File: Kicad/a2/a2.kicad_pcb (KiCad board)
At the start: 2 copper layers, 190 x 100 mm, 123 parts, among them J1 Conn_02x03_Odd_Even, J2 VGA, J3 AudioJack4, J4 Conn_02x17_Odd_Even, J6 Barrel Jack, J7 DE9_Plug, J8 DE9_Plug, SW1 Q, SW10 P, SW11 A, SW12 S, SW13 D, SW14 F, SW15 G, SW16 H, SW17 J, SW18 K, SW19 L, SW2 W, SW20 ENT, SW21 SHIFT, SW22 Z, SW23 X, SW24 C, SW25 V, SW26 B, SW27 N, SW28 M, SW29 SPACE, SW3 E, SW30 ALT, SW31 SW_Push, SW32 SW_SPDT, SW4 R, SW5 T, SW6 Y, SW7 U, SW8 I, SW9 O, U1 74HC590A, U10 74HC32, U11 74HC174, U12 74HC4520, U2 74HC590A, U3 62256, U4 SST39SF0x0, U5 W65C02SxP, U6 74HCT540, U7 74HC166, U8 74HC14, U9 74HC10, Y1 16Mhz

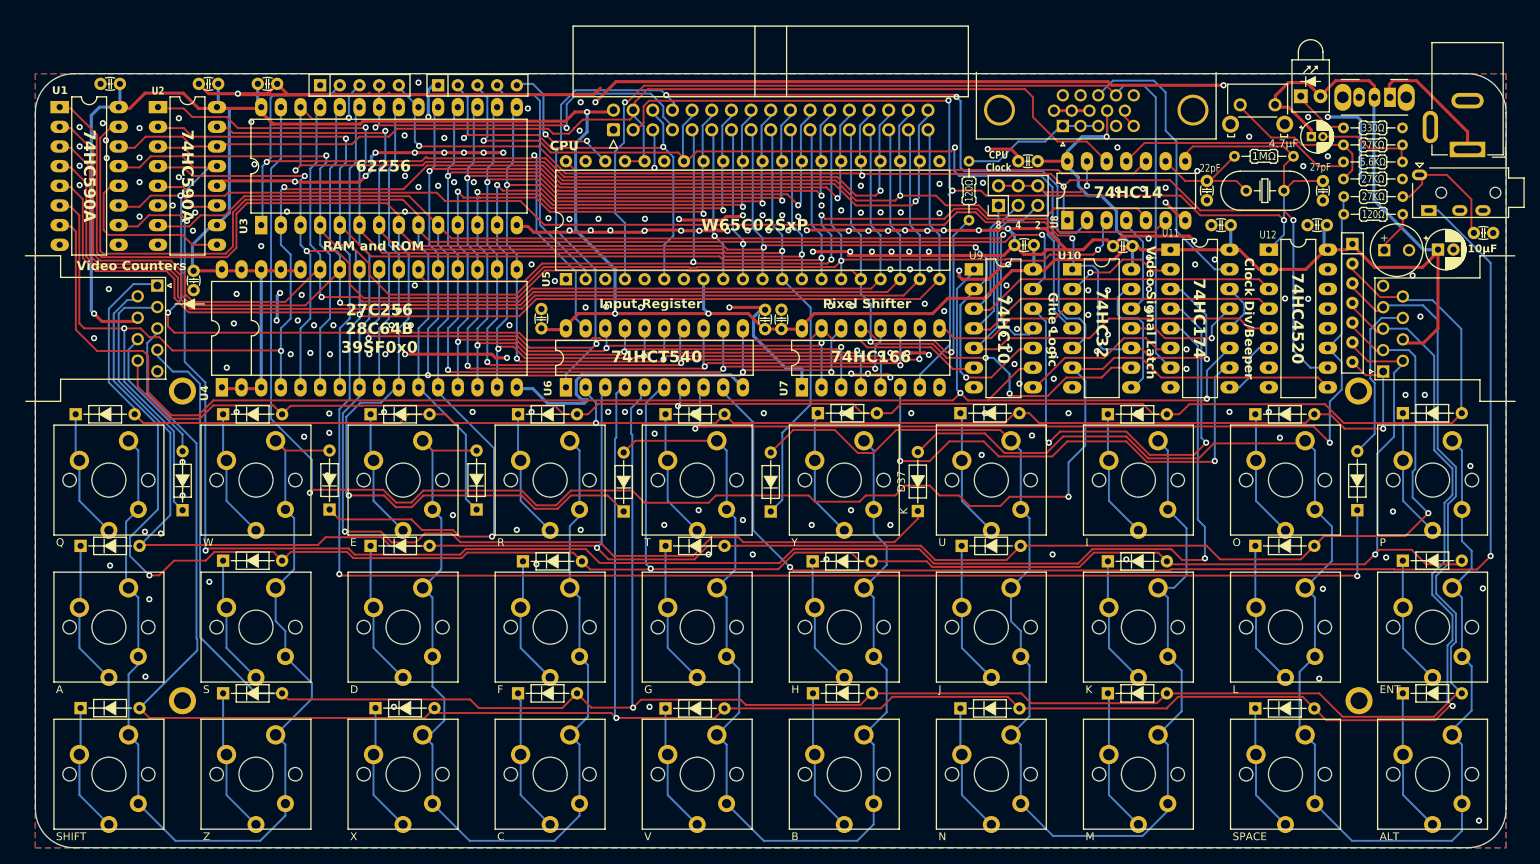
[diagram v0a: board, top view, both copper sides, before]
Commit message: add 2 more m2 screw posts
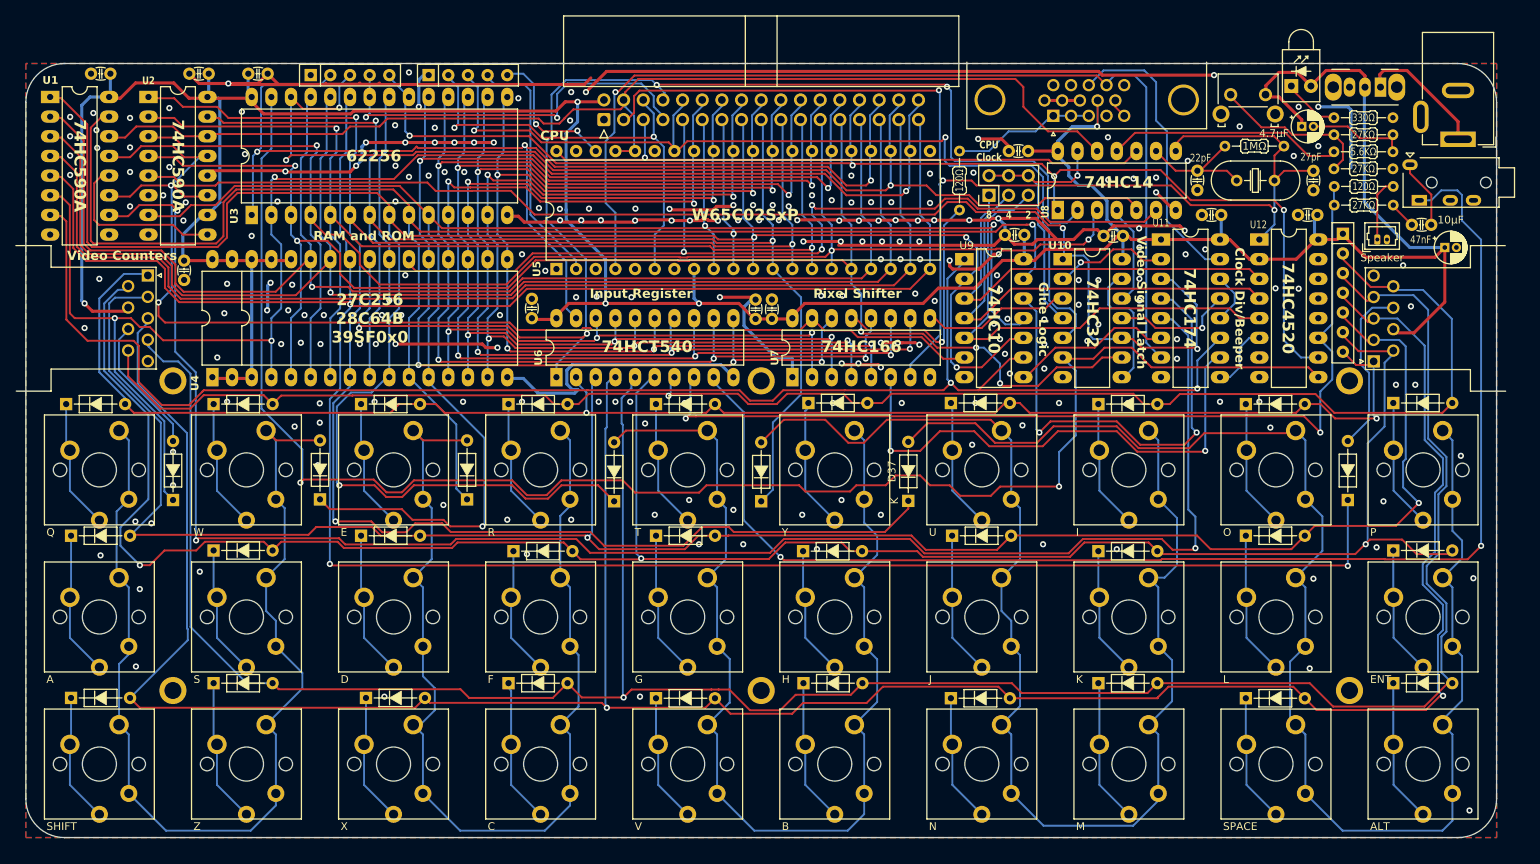
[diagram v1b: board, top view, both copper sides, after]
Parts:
- removed BZ1: Buzzer, Buzzer_Beeper:MagneticBuzzer_Kingstate_KCG0601
- added H5: M2, MountingHole:MountingHole_2.2mm_M2_ISO7380_Pad, F.Cu at (130.0, 116.0)
- added H6: M2, MountingHole:MountingHole_2.2mm_M2_ISO7380_Pad, F.Cu at (130.0, 76.0)
- added LS1: Speaker, Connector_Molex:Molex_PicoBlade_53047-0210_1x02_P1.25mm_Vertical, F.Cu at (209.6, 57.7)
- C16: footprint PCM_Capacitor_THT_AKL:CP_Radial_D5.0mm_P2.00mm -> PCM_Capacitor_THT_AKL:CP_Radial_D4.0mm_P1.50mm
- C17: value 100nF -> 47nF
- H1, H2, H3, H4: value MountingHole_Pad -> M2
- RN1: value R_Network06 -> 10KΩ
- RN2, RN3: value R_Network04 -> 1KΩ
- moved C17 5.61 mm to (216.6, 55.8), turned to 180 degrees
- moved R8 3.81 mm to (204.0, 50.9)
- moved D41 1.80 mm to (198.5, 37.9)
- moved D28 1.80 mm to (78.9, 117.0)
- moved C13 1.80 mm to (174.2, 57.3)
- moved C15 1.80 mm to (199.3, 54.6)
- moved D10 1.80 mm to (154.5, 78.9)
- moved D11 1.80 mm to (192.6, 79.0)
- moved D21 1.80 mm to (192.6, 96.0)
- moved D30 1.80 mm to (154.5, 117.0)
- moved D31 1.80 mm to (192.6, 117.0)
- moved J2 1.80 mm to (167.7, 41.8)
- moved U10 1.80 mm to (168.9, 60.3)
- moved U12 1.80 mm to (194.3, 57.7)
- moved D27 1.80 mm to (40.8, 117.0)
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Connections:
- net /AUDIN renamed /DataIn
- C17 pad 2: GND -> Net-(C17-Pad2)
- R6 pad 2: /DataOut -> Net-(C17-Pad2)
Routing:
- net /DataOut: track 16.5 -> 8.91 mm
- net VCC: track 443.8 -> 448.6 mm
- net /DataIn: track 167.0 -> 171.0 mm
- net Net-(C17-Pad2): track 0.00 -> 3.55 mm
- net /Speaker: track 4.95 -> 8.29 mm
- net /HROW 3: track 319.8 -> 321.5 mm
- net /HROW 2: track 335.8 -> 337.4 mm
- net /HROW 5: track 213.0 -> 214.1 mm
- net /V512: track 202.4 -> 203.5 mm
- net /HROW 0: track 204.5 -> 205.1 mm
- net GND: vias 227 -> 226

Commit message: Big a2 update
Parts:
- removed the C14 at (186.9, 54.6)
- removed the C3 at (199.8, 43.1)
- removed the R3 at (211.6, 48.6)
- removed the R4 at (204.0, 44.2)
- removed the R5 at (211.6, 46.4)
- added C17: 100nF, PCM_Capacitor_THT_AKL_Double:C_Disc_D3.0mm_W1.6mm_P2.50mm, F.Cu at (178.9, 67.9)
- added R1: 5.6KΩ, PCM_Resistor_THT_AKL_Double:R_Axial_DIN0204_L3.6mm_D1.6mm_P7.62mm_Horizontal, F.Cu at (204.0, 44.7)
- added U13: MCP100, PCM_Package_TO_SOT_THT_AKL:TO-92, F.Cu at (206.5, 48.6)
- J2: renamed from J4; value Conn_02x17_Odd_Even -> IDC 34
- R3: renamed from R7; footprint PCM_Resistor_THT_AKL_Double:R_Axial_DIN0204_L3.6mm_D1.6mm_P7.62mm_Horizontal -> PCM_Resistor_THT_AKL_Double:R_Axial_DIN0204_L3.6mm_D1.6mm_P5.08mm_Horizontal
- U8: value 74HC14 -> 74HCT04
- moved J3 39.1 mm to (198.1, 46.4), turned to 0 degrees
- moved C1 22.6 mm to (155.5, 67.9)
- moved C16 21.7 mm to (155.5, 46.4)
- moved C14 20.6 mm to (178.9, 56.5)
- moved U12 18.0 mm to (184.1, 75.5), turned to 90 degrees
- moved U10 17.4 mm to (160.7, 75.6), turned to 90 degrees
- moved R3 16.6 mm to (155.6, 70.5), turned to -90 degrees
- moved U11 12.4 mm to (184.2, 64.8), turned to 90 degrees
- moved R4 9.65 mm to (182.9, 52.3)
- moved C8 7.79 mm to (193.7, 47.2)
- moved U8 7.66 mm to (160.7, 54.0)
- moved Y1 7.51 mm to (184.2, 48.3)
- moved C7 7.13 mm to (179.4, 47.2)
- moved U9 6.29 mm to (160.7, 64.8), turned to 90 degrees
- moved C15 6.00 mm to (155.5, 57.1)
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- renumbered C11 to C1, C17 to C10, C8 to C11, C10 to C12, C15 to C14, C12 to C15, C13 to C16, C7 to C2, C9 to C3, C6 to C4, C4 to C5, C16 to C6, C1 to C7, C2 to C8, C5 to C9, D41 to D1, D6 to D12, D5 to D13, D16 to D14, D14 to D16, D13 to D17, D12 to D18, D17 to D19, D1 to D2, D18 to D20, D19 to D21, D20 to D22, D21 to D23, D22 to D24, D23 to D25, D24 to D26, D25 to D27, D26 to D28, D27 to D29, D38 to D3, D28 to D30, D29 to D31, D30 to D32, D31 to D33, D32 to D34, D33 to D35, D34 to D36, D35 to D37, D36 to D38, D39 to D4, D40 to D5, D37 to D6, J6 to J1, J1 to J3, J2 to J4, J3 to J5, J7 to J6, J8 to J7, R1 to R2, R2 to R4, R6 to R5, R8 to R6, RN2 to RN1, RN3 to RN2, RN1 to RN3, SW31 to SW1, SW6 to SW10, SW8 to SW11, SW10 to SW12, SW11 to SW13, SW13 to SW14, SW17 to SW16, SW19 to SW17, SW12 to SW18, SW14 to SW19, SW32 to SW2, SW16 to SW20, SW18 to SW21, SW20 to SW22, SW21 to SW23, SW23 to SW24, SW27 to SW26, SW29 to SW27, SW22 to SW28, SW24 to SW29, SW1 to SW3, SW26 to SW30, SW28 to SW31, SW30 to SW32, SW3 to SW4, SW7 to SW6, SW9 to SW7, SW2 to SW8, SW4 to SW9, U12 to U11, U11 to U12, U4 to U3, U3 to U4
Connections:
- net /COL 0 renamed Col 1
- net /COL 1 renamed Col 2
- net /COL 2 renamed Col 3
- net /COL 3 renamed Col 4
- net /COL 4 renamed Col 5
- net /HROW 0 renamed HRow 1
- net /HROW 1 renamed HRow 2
- net /HROW 2 renamed HRow 3
- net /HROW 3 renamed HRow 4
- net /HROW 4 renamed HRow 5
- net /HROW 5 renamed HRow 6
- net Net-(D5-A) renamed Joy 2
- net Net-(D6-A) renamed Joy 1
- net Net-(U11-D1) renamed /~{MRC!}
- C4 pad 1: GND -> VCC
- C4 pad 2: VCC -> GND
- C7 pad 1: Net-(C1-Pad1) -> Net-(C7-Pad1)
- J4 pad 13: /~{HSYNC}* -> /~{HSYNC}**
- R4 pad 1: Net-(C1-Pad1) -> Net-(C7-Pad1)
- SW1 pad 1: Net-(R3-Pad2) -> GND
- SW1 pad 2: VCC -> Net-(U13-VDD)
- U1 pad 11: /~{sload} -> /~{load}
- U1 pad 13: /~{sload} -> /~{load}
- U10 pad 1: /H32 -> /~{H32}
- U10 pad 11: Net-(U11-D4) -> /~{HSYNC!}
- U10 pad 2: /H32* -> /~{load}
- U10 pad 3: Net-(U7-Clr) -> /~{sload}
- U12 pad 10: /V512* -> /~{HSYNC}
- U12 pad 11: /V512 -> /~{HSYNC!}
- U12 pad 12: /~{HSYNC} -> /~{HSYNC}*
- U12 pad 13: Net-(U11-D4) -> /~{HSYNC}
- U12 pad 14: /~{HSYNC} -> /~{HSYNC}*
- U12 pad 15: /~{HSYNC}* -> /~{HSYNC}**
- U12 pad 2: /H32* -> /V512*
- U12 pad 3: /H32 -> /V512
- U12 pad 6: Net-(U11-D2) -> /~{VSYNC!}
- U2 pad 11: /~{sload} -> /~{load}
- U2 pad 13: /~{sload} -> /~{load}
- U2 pad 6: unconnected-(U2-Q6-Pad6) -> /V1
- U7 pad 9: Net-(U7-Clr) -> VCC
- U8 pad 1: /A15 -> /H32
- U8 pad 10: /~{RESET} -> /~{A15}
- U8 pad 11: Net-(R5-Pad2) -> /A15
- U8 pad 12: /ø2 -> /~{A13}
- U8 pad 13: /ø1 -> /A13
- U8 pad 2: /~{A15} -> /~{H32}
- U8 pad 5: /A13 -> Net-(C7-Pad1)
- U8 pad 6: /~{A13} -> /M16
- U8 pad 8: /M16 -> /ø2
- U8 pad 9: Net-(C1-Pad1) -> /ø1
- U9 pad 10: /A2 -> /M4
- U9 pad 11: /A0 -> /M2
- U9 pad 3: /M8 -> /V512
- U9 pad 4: /M4 -> /A2
- U9 pad 5: /M2 -> /A0
- U9 pad 6: /~{sload} -> /~{VSYNC!}
- U9 pad 8: Net-(U11-D2) -> /~{load}
- U9 pad 9: /V512 -> /M8
- Y1 pad 1: Net-(C1-Pad1) -> Net-(C7-Pad1)
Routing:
- net /~{load}: track 0.00 -> 199.8 mm, vias 0 -> 4
- net /~{sload}: track 158.9 -> 32.7 mm, vias 2 -> 1
- net /~{HSYNC}**: track 0.00 -> 80.8 mm, vias 0 -> 3
- net GND: track 443.8 -> 385.3 mm, vias 226 -> 210
- net /~{VSYNC!}: track 0.00 -> 36.2 mm, vias 0 -> 1
- net /~{HSYNC!}: track 0.00 -> 34.6 mm, vias 0 -> 2
- net Net-(J4-Pad1): track 18.6 -> 52.7 mm, vias 0 -> 1
- net /~{HSYNC}*: track 37.5 -> 6.39 mm
- net /ø1: track 35.7 -> 66.4 mm, vias 1 -> 0
- net /~{RESET}: track 80.5 -> 110.9 mm
- net Net-(R5-Pad2): track 30.2 -> 0.00 mm
- net /H32: track 165.3 -> 138.3 mm, vias 2 -> 1
- net /~{VSYNC}: track 131.2 -> 156.6 mm, vias 1 -> 2
- net /~{H32}: track 0.00 -> 23.7 mm
- net Net-(C7-Pad1): track 0.00 -> 22.6 mm
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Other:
- board text added: "Clk/Beep"
- board text added: "Clock"
- board text added: "MicroMicro v2 - Apr 2025"
- board text added: "Sig Buffer"
- board text removed: "CPU Clock"
- board text removed: "Clock Div/Beeper"
- board text removed: "Glue Logic"
- board text removed: "MicroMicro v1 - Jan 2025"
- board text removed: "Video Signal Latch"

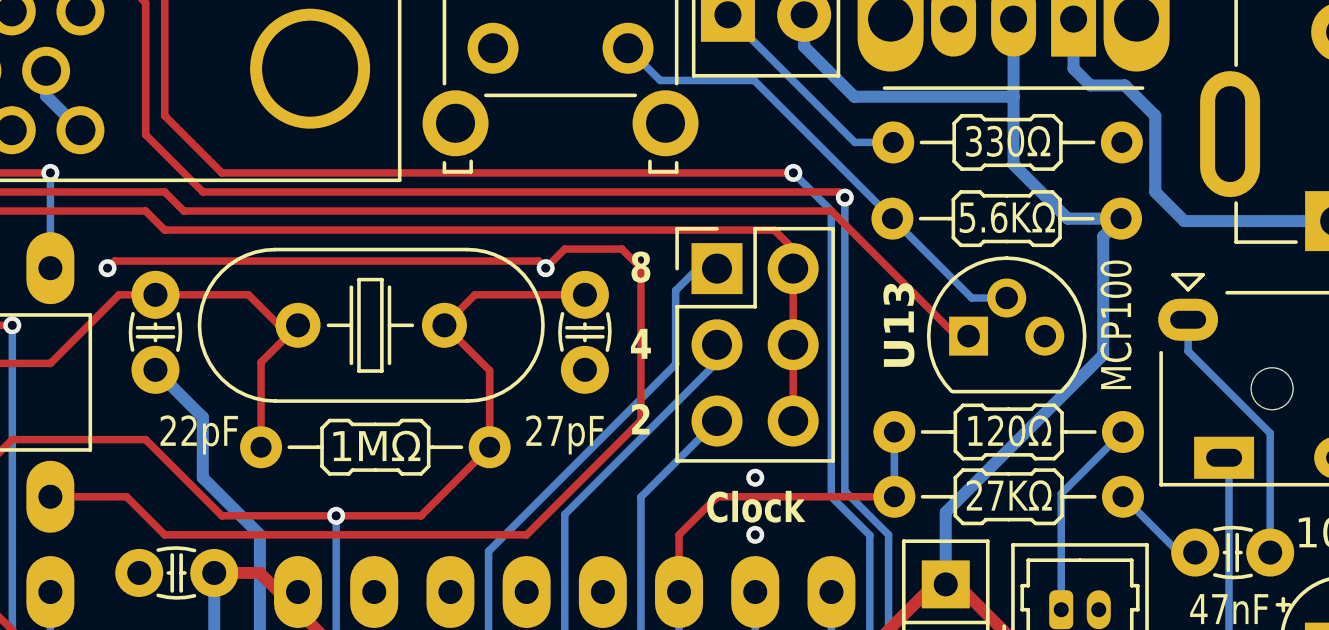
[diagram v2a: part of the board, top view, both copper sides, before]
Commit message: Specify MCP100 H boundout version (why are there 2)
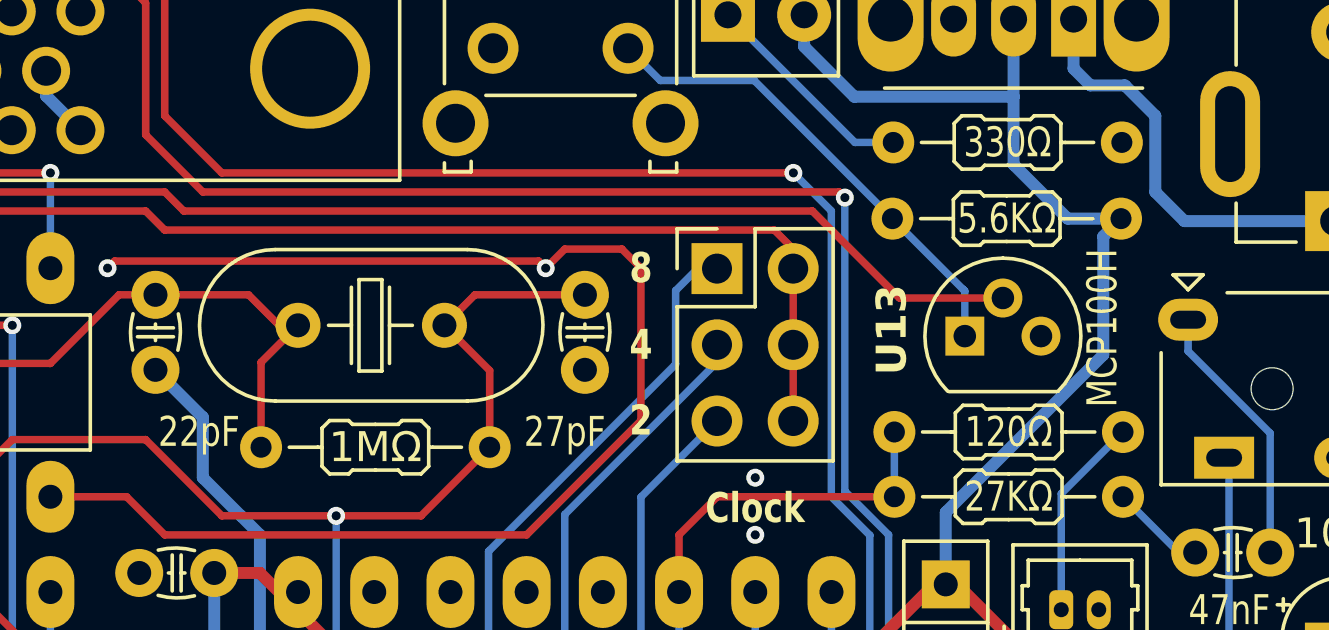
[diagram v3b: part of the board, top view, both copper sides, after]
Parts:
- U13: value MCP100 -> MCP100H; footprint PCM_Package_TO_SOT_THT_AKL:TO-92 -> Package_TO_SOT_THT:TO-92
- moved U13 0.13 mm to (206.4, 48.6)
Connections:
- U13 pad 1: /~{RESET} -> Net-(U13-VDD)
- U13 pad 2: Net-(U13-VDD) -> /~{RESET}
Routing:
- net /~{RESET}: track 110.9 -> 111.5 mm

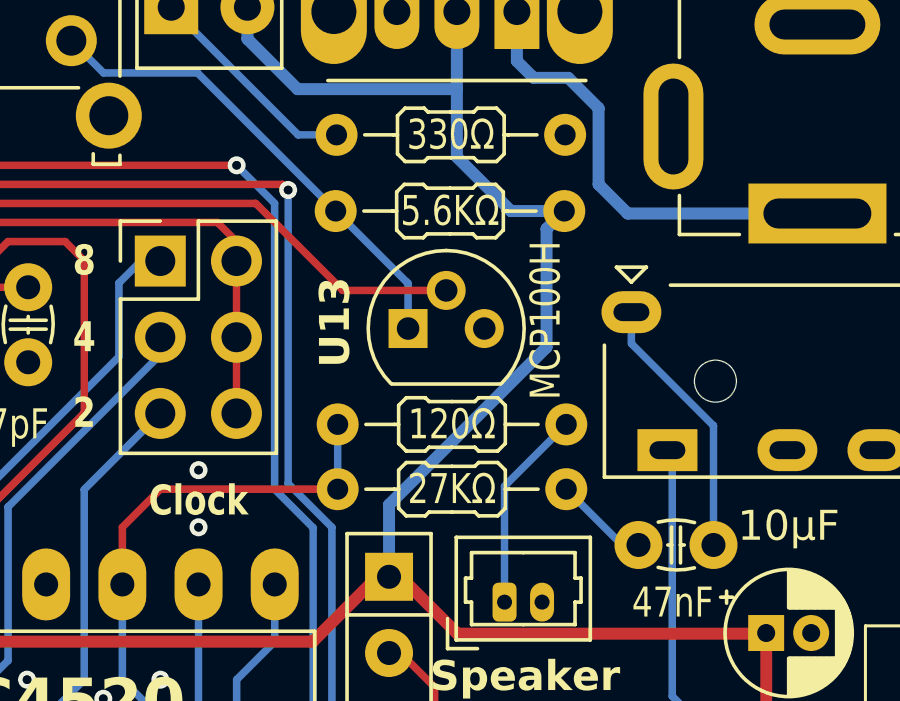
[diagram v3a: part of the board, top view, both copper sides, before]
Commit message: tweak resitor values
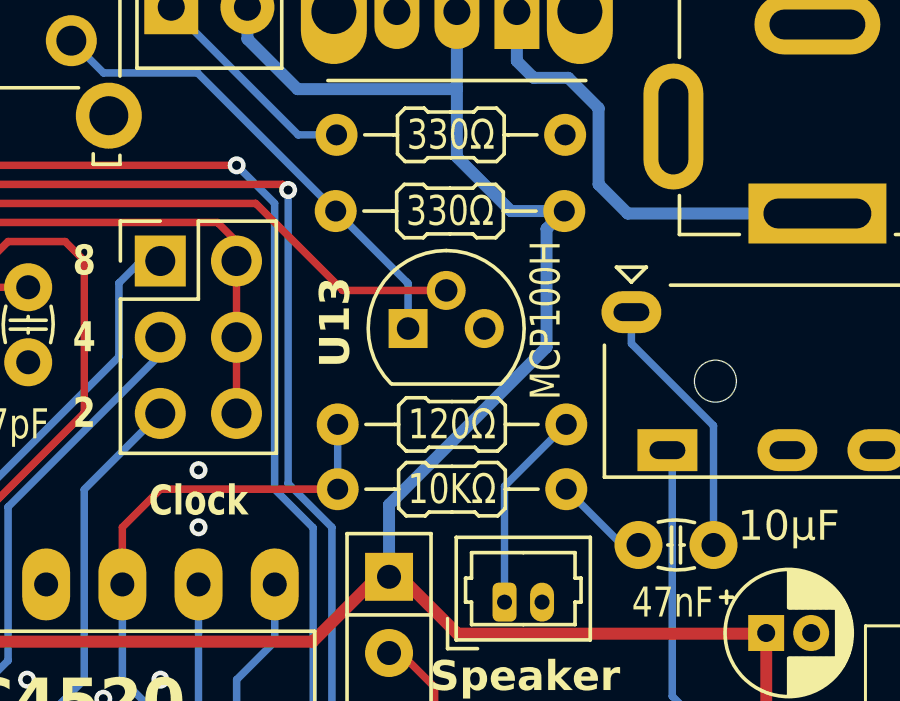
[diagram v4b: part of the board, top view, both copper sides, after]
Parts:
- R1: value 5.6KΩ -> 330Ω
- R5: value 27KΩ -> 10KΩ
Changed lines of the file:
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@@
 			)
 		)
-		(property "Value" "5.6KΩ"
+		(property "Value" "330Ω"
 			(at 3.81 0 0)
 			(layer "F.SilkS")
@@
 			)
 		)
-		(property "Value" "27KΩ"
+		(property "Value" "10KΩ"
 			(at 3.81 0 0)
 			(layer "F.SilkS")
